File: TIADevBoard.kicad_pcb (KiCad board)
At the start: 2 copper layers, 44.5 x 45.7 mm, 40 parts, among them J1 Screw_Terminal_01x02, J2 Conn_Coaxial, J3 Conn_Coaxial, J4 Conn_02x03_Counter_Clockwise, U1 MC33063AD, U2 OPA2387, U3 ADP3330-3, U4 ADP7183

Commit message: added second SMA connector for Vin+ terminal
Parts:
- added J5: Conn_Coaxial, my_library_foot:CON-SMA-EDGE-S, F.Cu at (92.3, 107.5)
- moved C12 1.46 mm to (90.9, 105.0), turned to 180 degrees
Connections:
- net /VIN renamed /VIN-
- U2 pad 3: GND -> /VIN+
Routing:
- net /VIN+: track 0.00 -> 10.7 mm
- net GND: track 28.0 -> 32.2 mm, vias 15 -> 16
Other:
- board text added: "VIN+"
- board text added: "VIN-"
- board text removed: "VIN"

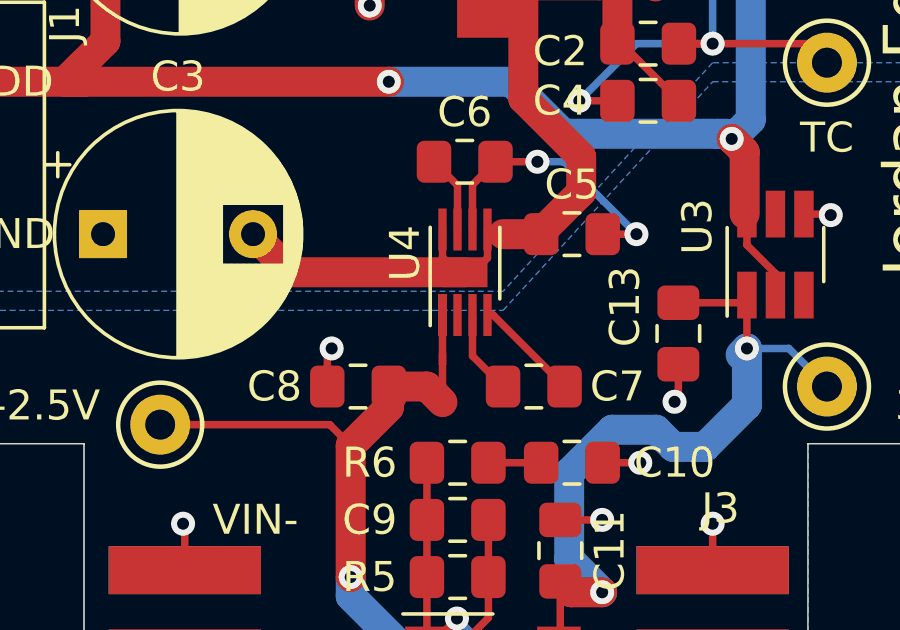
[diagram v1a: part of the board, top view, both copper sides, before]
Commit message: fixed some errors in version 3 of PCB, updated the README to that effect.
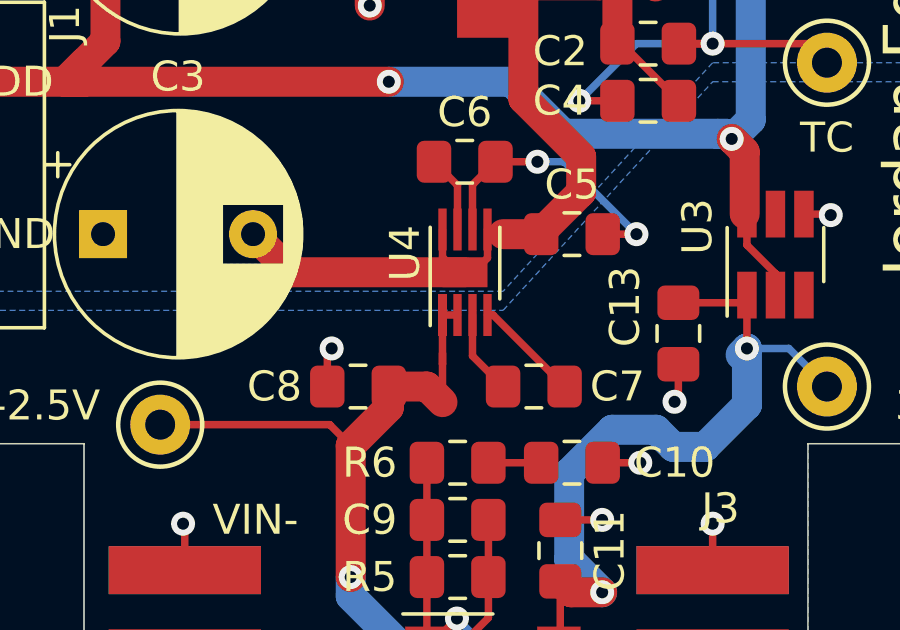
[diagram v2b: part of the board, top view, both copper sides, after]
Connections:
- U4 pad 2: Net-(U4-Pad2) -> /-2.5V
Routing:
- net /-2.5V: track 28.1 -> 28.6 mm

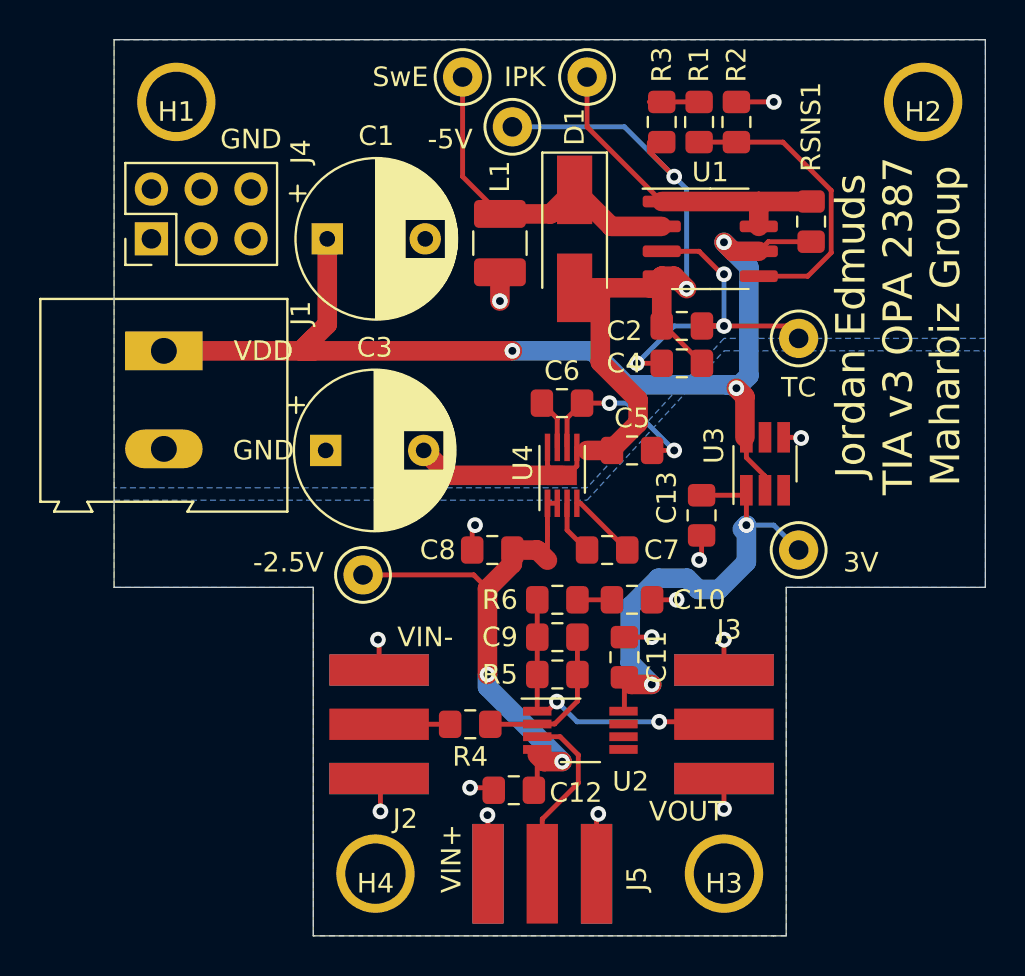
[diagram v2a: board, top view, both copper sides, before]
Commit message: partial redesign of TIA v4, removed boost/buck converter, -2.5V linear regulator, added in second opamp in unity gain configuration with bias voltage. Layout not complete.
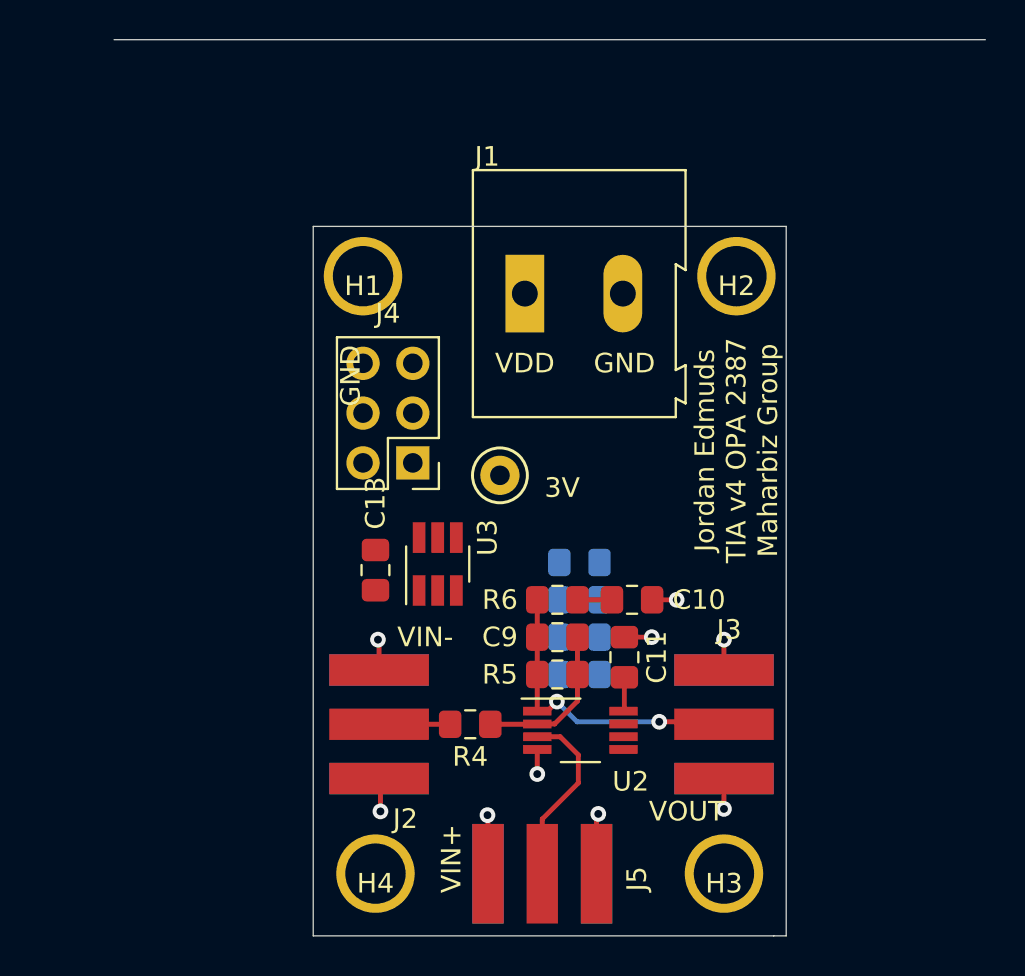
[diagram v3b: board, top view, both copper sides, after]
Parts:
- removed C12: 470nF, Capacitor_SMD:C_0805_2012Metric_Pad1.15x1.40mm_HandSolder
- removed C2, C4: 100pF, Capacitor_SMD:C_0805_2012Metric_Pad1.15x1.40mm_HandSolder
- removed C3: 220uF, Capacitor_THT:CP_Radial_D8.0mm_P5.00mm
- removed C5, C8: 10uF, Capacitor_SMD:C_0805_2012Metric_Pad1.15x1.40mm_HandSolder
- removed C6, C7: 1uF, Capacitor_SMD:C_0805_2012Metric_Pad1.15x1.40mm_HandSolder
- removed D1: D_Schottky, Diode_SMD:D_SMA_Handsoldering
- removed L1: 100uH, Inductor_SMD:L_1210_3225Metric_Pad1.42x2.65mm_HandSolder
- removed RSNS1: 1.5R, Resistor_SMD:R_0805_2012Metric_Pad1.15x1.40mm_HandSolder
- removed TP2: IPK, my_library_foot:TestPoint_Keystone_5000-5004_Miniature
- removed TP3: -5V, my_library_foot:TestPoint_Keystone_5000-5004_Miniature
- removed TP4: -2.5V, my_library_foot:TestPoint_Keystone_5000-5004_Miniature
- removed TP5: TC, my_library_foot:TestPoint_Keystone_5000-5004_Miniature
- removed TP6: SwE, my_library_foot:TestPoint_Keystone_5000-5004_Miniature
- removed U1: MC33063AD, Package_SO:SOIC-8_3.9x4.9mm_P1.27mm
- removed U4: ADP7183, Package_CSP:LFCSP-8-1EP_2x2mm_P0.5mm_EP1.5x1.0mm
- C1: value 100uF -> C; footprint Capacitor_THT:CP_Radial_D8.0mm_P5.00mm -> Capacitor_SMD:C_0805_2012Metric_Pad1.15x1.40mm_HandSolder; moved to B.Cu
- C11: value 470nF -> 1uF
- R1: value 1k -> 10k; moved to B.Cu
- R2: moved to B.Cu
- R3: value 1k -> 0R; moved to B.Cu
- U3: value ADP3330-3 -> ADP3330-3.3
- moved R2 27.5 mm to (94.2, 97.2), turned to 180 degrees
- moved C1 25.7 mm to (94.2, 99.1), turned to 180 degrees
- moved R3 24.7 mm to (94.2, 95.2), turned to 0 degrees
- moved R1 23.3 mm to (94.2, 93.3), turned to 0 degrees
- moved J1 18.6 mm to (91.4, 79.6), turned to 0 degrees
- moved J4 17.6 mm to (85.7, 88.3), turned to 180 degrees
- moved U3 17.5 mm to (87.0, 93.4)
- moved C13 16.9 mm to (83.8, 93.7), turned to 90 degrees
- moved TP1 15.7 mm to (90.2, 88.9)
- moved H1 13.0 mm to (83.2, 78.7)
- moved H2 13.0 mm to (102.2, 78.7)
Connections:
- C1 pad 1: VDD -> Net-(C1-Pad1)
- C11 pad 2: /3V -> +3V3
- C13 pad 1: /3V -> +3V3
- J2 pad 2: GND -> /VGUARD
- R1 pad 1: Net-(R1-Pad1) -> +3V3
- R1 pad 2: /VFB -> Net-(C1-Pad1)
- R2 pad 1: /VFB -> Net-(C1-Pad1)
- R3 pad 1: -5V -> /VIN+
- R3 pad 2: Net-(R1-Pad1) -> Net-(C1-Pad1)
- TP1 pad 1: /3V -> +3V3
- U2 pad 4: /-2.5V -> GND
- U2 pad 5: Net-(U2-Pad5) -> Net-(C1-Pad1)
- U2 pad 6: Net-(U2-Pad6) -> /VGUARD
- U2 pad 7: Net-(U2-Pad7) -> /VGUARD
- U2 pad 8: /3V -> +3V3
- U3 pad 1: /3V -> +3V3
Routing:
- net VDD: track 56.0 -> 0.00 mm, vias 3 -> 0
- net -5V: track 53.8 -> 0.00 mm, vias 2 -> 0
- net /-2.5V: track 28.6 -> 0.00 mm, vias 2 -> 0
- net /3V: track 24.6 -> 0.00 mm, vias 2 -> 0
- net /TC: track 20.1 -> 0.00 mm, vias 3 -> 0
- net GND: track 32.2 -> 13.1 mm, vias 16 -> 7
- net /SwE: track 17.3 -> 0.00 mm
- net /Ipk: track 16.8 -> 0.00 mm
- net /VFB: track 15.1 -> 0.00 mm
- net Net-(C7-Pad2): track 3.56 -> 0.00 mm
- net /VGUARD: track 0.00 -> 3.30 mm, vias 0 -> 2
- net Net-(C7-Pad1): track 2.81 -> 0.00 mm
- net Net-(C6-Pad1): track 2.58 -> 0.00 mm
- net Net-(R1-Pad1): track 2.54 -> 0.00 mm
- net +3V3: track 0.00 -> 1.75 mm
- removed copper zone on B.Cu, net GND
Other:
- outline, holes or cut-outs redrawn
- board text added: "Jordan Edmuds TIA v4 OPA 2387 Maharbiz Group"
- board text removed: "Jordan Edmuds TIA v3 OPA 2387 Maharbiz Group"

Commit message: modified TIA dev board to use a single supply of 3.3V, and optionally bias both sides of the diode at VDD/2 using one of the opamps to drive the guard shield. Should work just as well as grounding it up to ~MHz.
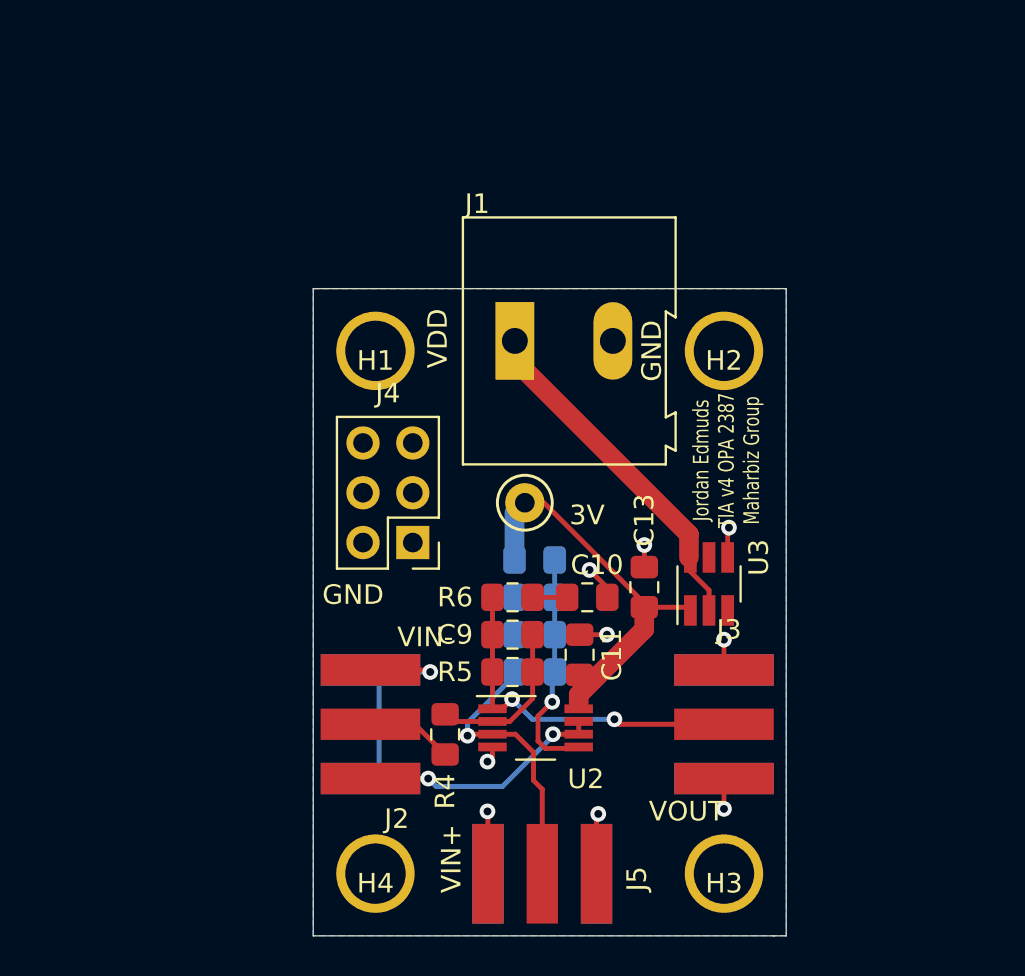
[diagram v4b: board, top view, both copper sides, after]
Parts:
- moved U3 13.9 mm to (100.8, 94.4)
- moved C13 13.7 mm to (97.5, 94.6)
- moved C1 4.55 mm to (91.9, 95.1)
- moved R3 4.33 mm to (92.0, 98.9)
- moved J4 4.06 mm to (85.7, 92.3)
- moved H2 3.86 mm to (101.6, 82.5)
- moved H1 3.86 mm to (83.8, 82.5)
- moved J1 2.47 mm to (90.9, 82.0)
- moved C11 2.29 mm to (94.2, 98.1)
- moved C10 2.29 mm to (94.6, 95.1)
- moved C9 2.29 mm to (90.8, 97.0)
- moved R1 2.29 mm to (91.9, 93.2)
- moved R2 2.29 mm to (91.9, 97.0)
- moved R5 2.29 mm to (90.8, 98.9)
- moved R6 2.29 mm to (90.8, 95.1)
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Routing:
- net /VGUARD: track 3.30 -> 27.3 mm, vias 2 -> 3
- net +3V3: track 1.75 -> 22.0 mm
- net VDD: track 0.00 -> 17.8 mm
- net Net-(C1-Pad1): track 0.00 -> 11.9 mm, vias 0 -> 1
- net /VIN+: track 10.7 -> 15.6 mm, vias 0 -> 1
- net GND: track 13.1 -> 16.1 mm, vias 7 -> 9
- net /VOUT: track 15.9 -> 18.2 mm
- net /VIN-: track 3.62 -> 4.45 mm
- added copper zone on B.Cu, net GND
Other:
- board size 44.5 x 45.7 mm -> 24.1 x 33 mm
